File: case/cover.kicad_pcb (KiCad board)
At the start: 2 copper layers, 20.1 x 62.5 mm, 2 parts

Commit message: update case files
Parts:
- added G***: LOGO, pica:logo, F.Cu at (132.2, 102.7)
- added G***: LOGO, pica:logo_mirror, B.Cu at (132.2, 102.7)
- added RE1: RotaryEncoder_Switch, pica:EC11_Hole, F.Cu at (133.0, 85.0)
- H6, H7: footprint kbd:thread_m2 -> kbd:M2_Hole_TH
- moved H7 61.6 mm to (138.9, 117.7)
- moved H6 61.3 mm to (126.8, 117.7)
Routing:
- net (no net): vias 0 -> 1
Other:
- board size 20.1 x 62.5 mm -> 20 x 55 mm
- board text added: "JLCJLCJLCJLC"
- board text added: "PicaPica"
- board text added: "github.com/zzeneg/pica40"

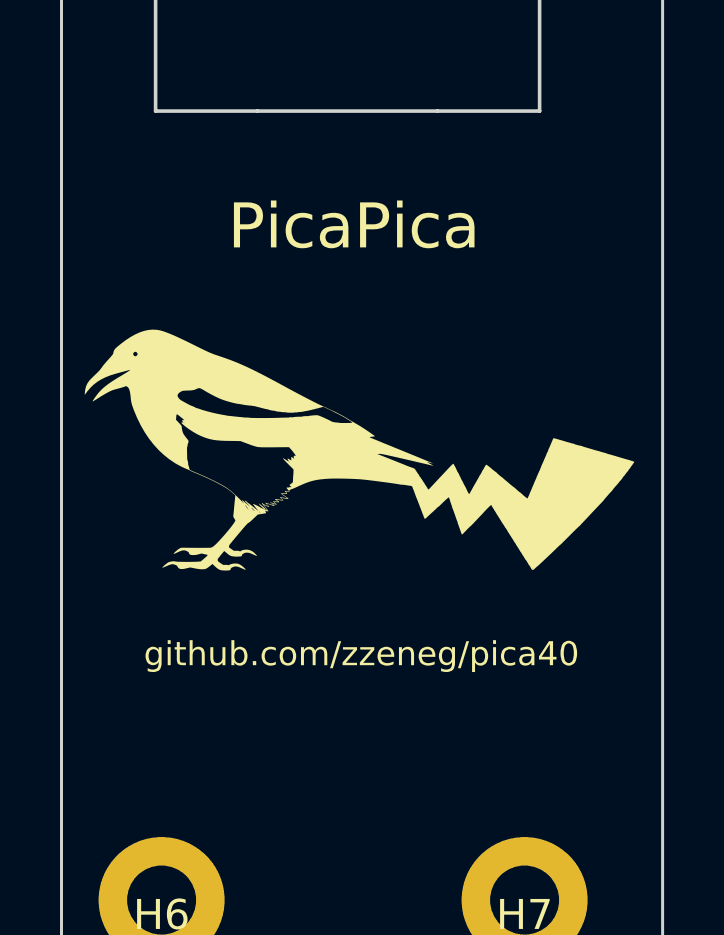
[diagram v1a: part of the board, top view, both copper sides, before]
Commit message: remove logos from top
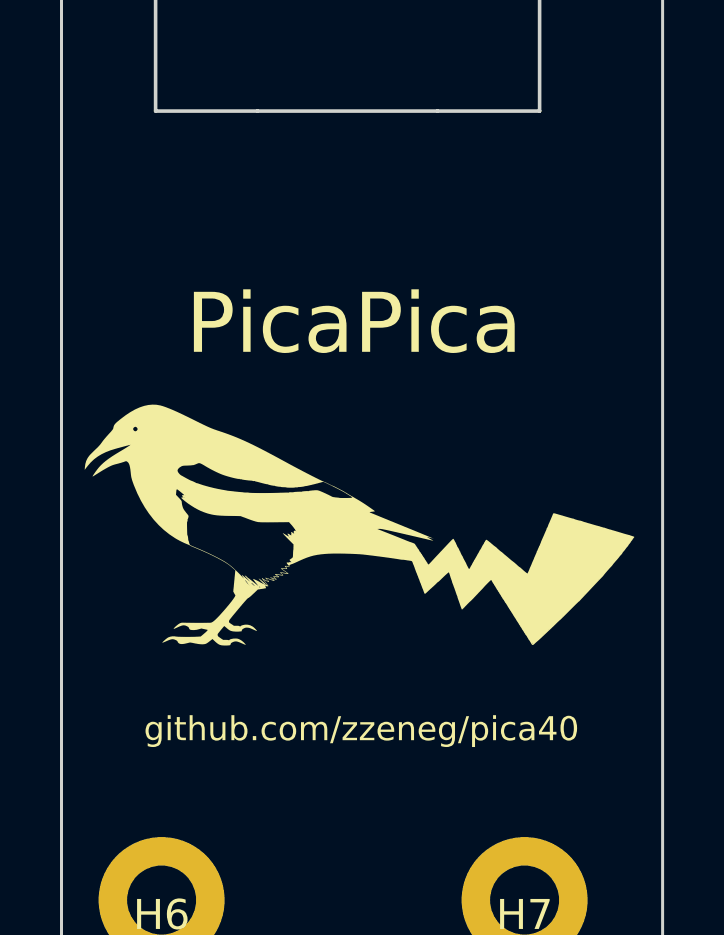
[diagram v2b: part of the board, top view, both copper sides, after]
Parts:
- moved G*** 2.50 mm to (132.2, 105.2) (x2)
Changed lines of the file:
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@@
   )
   (footprint "pica:logo" (layer "F.Cu")
-    (at 132.25 102.695176)
+    (at 132.25 105.195176)
     (attr board_only exclude_from_pos_files exclude_from_bom)
     (fp_text reference "G***" (at 0 0) (layer "F.SilkS") hide
@@
   )
   (footprint "pica:logo_mirror" (layer "B.Cu")
-    (at 132.25 102.695176 180)
+    (at 132.25 105.195176 180)
     (attr board_only exclude_from_pos_files exclude_from_bom)
     (fp_text reference "G***" (at 0 0) (layer "B.SilkS") hide
@@
   (gr_line (start 142.037034 121) (end 125 121) (layer "Edge.Cuts") (width 0.1))
   (gr_arc (start 123.5 67.5) (mid 123.939342 66.439341) (end 125.000001 66) (layer "Edge.Cuts") (width 0.1))
-  (gr_text "PicaPica" (at 133.25 95.25) (layer "B.SilkS")
-    (effects (font (size 1.5 1.5) (thickness 0.3)) (justify mirror))
+  (gr_text "PicaPica" (at 133.25 98.5) (layer "B.SilkS")
+    (effects (font (size 2 2) (thickness 0.3)) (justify mirror))
   )
-  (gr_text "github.com/zzeneg/pica40" (at 133.5 109.5) (layer "B.SilkS")
+  (gr_text "github.com/zzeneg/pica40" (at 133.5 112) (layer "B.SilkS")
     (effects (font (size 0.8 0.8) (thickness 0.15)) (justify mirror))
   )
@@
     (effects (font (size 0.8 0.8) (thickness 0.15)) (justify mirror))
   )
-  (gr_text "PicaPica" (at 133.25 95.25) (layer "F.SilkS")
-    (effects (font (size 1.5 1.5) (thickness 0.3)))
+  (gr_text "PicaPica" (at 133.25 98.5) (layer "F.SilkS")
+    (effects (font (size 2 2) (thickness 0.3)))
   )
-  (gr_text "github.com/zzeneg/pica40" (at 133.5 109.5) (layer "F.SilkS")
+  (gr_text "github.com/zzeneg/pica40" (at 133.5 112) (layer "F.SilkS")
     (effects (font (size 0.8 0.8) (thickness 0.15)))
   )
-  (via (at 125.999998 99.445175) (size 0.8) (drill 0.4) (layers "F.Cu" "B.Cu") (free) (net 0))
+  (via (at 125.999998 101.945175) (size 0.8) (drill 0.4) (layers "F.Cu" "B.Cu") (free) (net 0))
 )

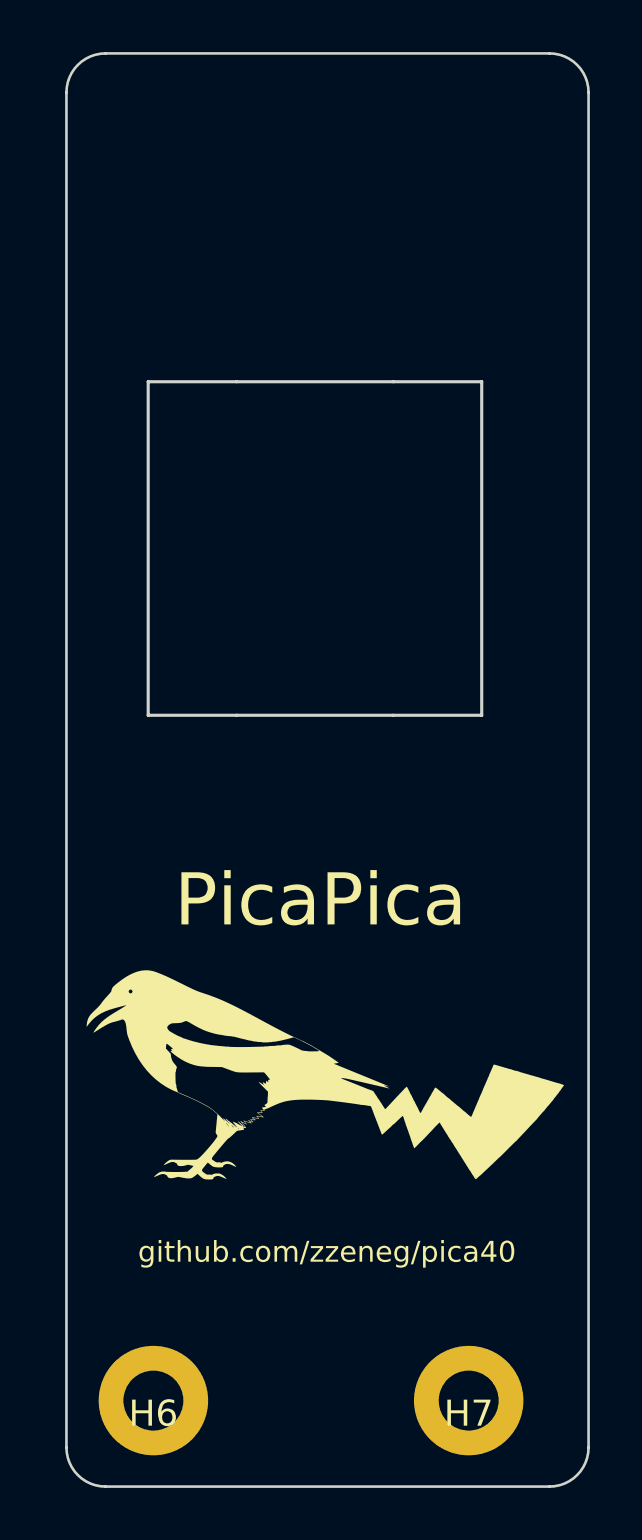
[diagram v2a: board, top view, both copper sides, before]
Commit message: update cases, extra hole on right side
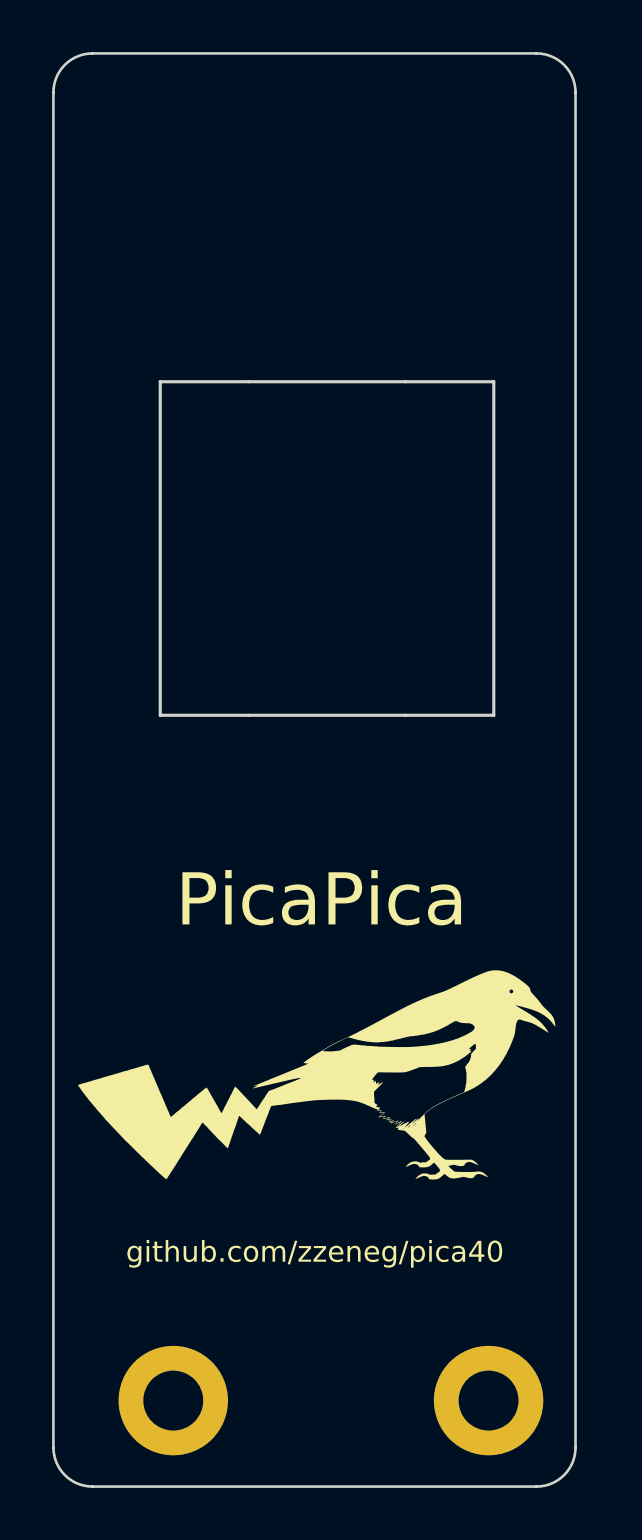
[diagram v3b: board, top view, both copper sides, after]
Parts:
- G***: moved to F.Cu
- G***, H6, H7, RE1: moved to B.Cu
- moved H6 12.9 mm to (139.7, 117.7), turned to 180 degrees
- moved H7 11.3 mm to (127.6, 117.7), turned to 180 degrees
- moved G*** 2.04 mm to (134.3, 105.2), turned to 0 degrees
- moved G*** 2.04 mm to (134.3, 105.2), turned to 180 degrees
- moved RE1 0.46 mm to (133.5, 85.0)

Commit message: update case files
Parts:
- removed G***: LOGO, pica:logo_mirror
- removed G***: LOGO, pica:logo
- removed H6, H7: MountingHole, kbd:M2_Hole_TH
- removed RE1: RotaryEncoder_Switch, pica:EC11_Hole
- added Ref**: Val**, kbd:thread_m2, F.Cu at (112.8, 76.5)
- added Ref**: Val**, kbd:thread_m2, F.Cu at (104.0, 76.5)
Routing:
- net (no net): vias 1 -> 0
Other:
- board size 20 x 55 mm -> 20 x 28.5 mm
- board text removed: "JLCJLCJLCJLC"
- board text removed: "PicaPica"
- board text removed: "github.com/zzeneg/pica40"

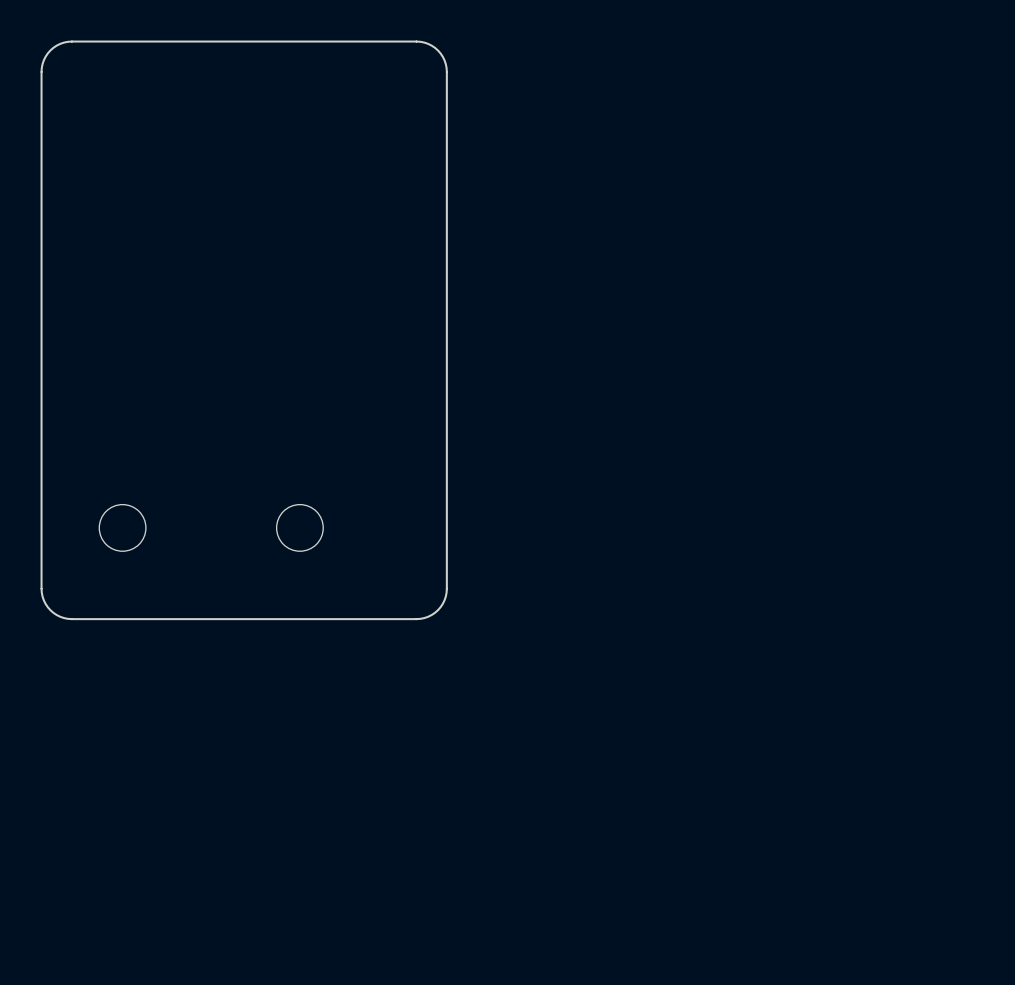
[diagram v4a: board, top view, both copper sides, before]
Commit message: update cover
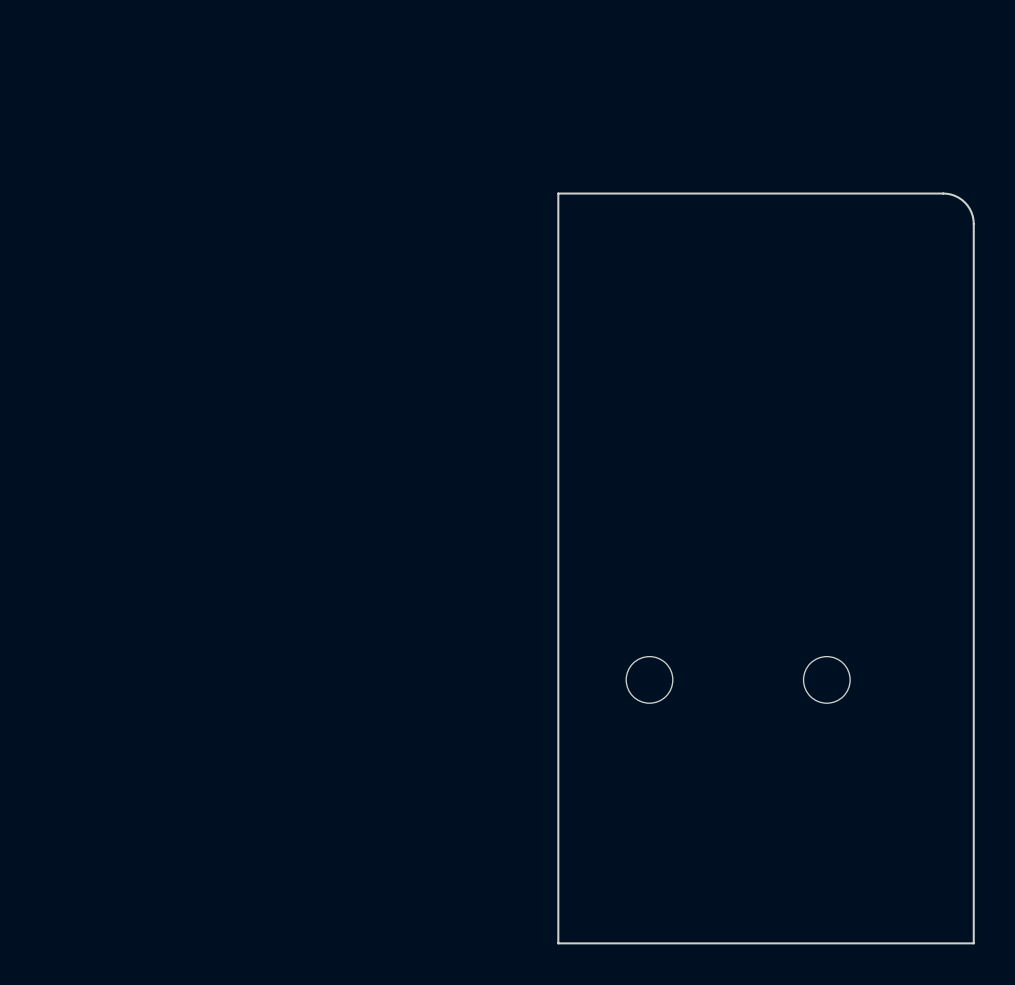
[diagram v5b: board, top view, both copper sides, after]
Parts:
- removed Ref** (x2): Val**, kbd:thread_m2
- added H6: MountingHole, kbd:thread_m2, F.Cu at (130.0, 84.0)
- added H7: MountingHole, kbd:thread_m2, F.Cu at (138.8, 84.0)
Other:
- board size 20 x 28.5 mm -> 20.5 x 37 mm
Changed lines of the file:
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@@
   (net 0 "")
   (footprint "kbd:thread_m2" (layer "F.Cu")
-    (at 112.75 76.5)
+    (at 138.75 84)
     (descr "Mounting Hole 2.2mm, no annular, M2")
     (tags "mounting hole 2.2mm no annular m2")
-    (attr exclude_from_pos_files exclude_from_bom)
-    (fp_text reference "Ref**" (at -0.95 -0.55) (layer "F.Fab") hide
+    (property "Sheetfile" "left.kicad_sch")
+    (property "Sheetname" "")
+    (attr exclude_from_pos_files)
+    (fp_text reference "H7" (at -0.95 -0.55) (layer "F.Fab") hide
       (effects (font (size 1 1) (thickness 0.15)))
     )
-    (fp_text value "Val**" (at 0 0.55) (layer "F.Fab") hide
+    (fp_text value "MountingHole" (at 0 0.55) (layer "F.Fab") hide
       (effects (font (size 1 1) (thickness 0.15)))
     )
@@
   )
   (footprint "kbd:thread_m2" (layer "F.Cu")
-    (at 104 76.5)
+    (at 130 84)
     (descr "Mounting Hole 2.2mm, no annular, M2")
     (tags "mounting hole 2.2mm no annular m2")
-    (attr exclude_from_pos_files exclude_from_bom)
-    (fp_text reference "Ref**" (at -0.95 -0.55) (layer "F.Fab") hide
+    (property "Sheetfile" "left.kicad_sch")
+    (property "Sheetname" "")
+    (attr exclude_from_pos_files)
+    (fp_text reference "H6" (at -0.95 -0.55) (layer "F.Fab") hide
       (effects (font (size 1 1) (thickness 0.15)))
     )
-    (fp_text value "Val**" (at 0 0.55) (layer "F.Fab") hide
+    (fp_text value "MountingHole" (at 0 0.55) (layer "F.Fab") hide
       (effects (font (size 1 1) (thickness 0.15)))
     )
     (pad "" np_thru_hole circle locked (at 0 0) (size 2.3 2.3) (drill 2.3) (layers *.Cu *.Mask))
   )
-  (gr_arc (start 120 79.5) (mid 119.56066 80.56066) (end 118.5 81) (layer "Edge.Cuts") (width 0.1))
-  (gr_arc (start 118.5 52.5) (mid 119.56066 52.93934) (end 120 54) (layer "Edge.Cuts") (width 0.1))
-  (gr_line (start 101.5 52.5) (end 118.5 52.5) (layer "Edge.Cuts") (width 0.1))
-  (gr_arc (start 101.5 81) (mid 100.43934 80.56066) (end 100 79.5) (layer "Edge.Cuts") (width 0.1))
-  (gr_line (start 118.5 81) (end 101.5 81) (layer "Edge.Cuts") (width 0.1))
-  (gr_line (start 100 79.5) (end 100 54) (layer "Edge.Cuts") (width 0.1))
-  (gr_arc (start 100 54) (mid 100.43934 52.93934) (end 101.5 52.5) (layer "Edge.Cuts") (width 0.1))
-  (gr_line (start 120 54) (end 120 79.5) (layer "Edge.Cuts") (width 0.1))
+  (gr_line (start 125.5 97) (end 125.5 60) (layer "Edge.Cuts") (width 0.1))
+  (gr_arc (start 144.5 60) (mid 145.56066 60.43934) (end 146 61.5) (layer "Edge.Cuts") (width 0.1))
+  (gr_line (start 146 97) (end 146 61.5) (layer "Edge.Cuts") (width 0.1))
+  (gr_line (start 146 97) (end 125.5 97) (layer "Edge.Cuts") (width 0.1))
+  (gr_line (start 144.5 60) (end 125.5 60) (layer "Edge.Cuts") (width 0.1))
 )
